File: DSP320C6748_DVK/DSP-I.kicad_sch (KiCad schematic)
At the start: 37 parts, among them IC1 SN74LVC1G11DBVR, J1 USB_A, J2 JTAG, U1 TMS320C6748EZWT4, Y1 ASE-24.000MHZ-LC-T, Y2 FX135A-327

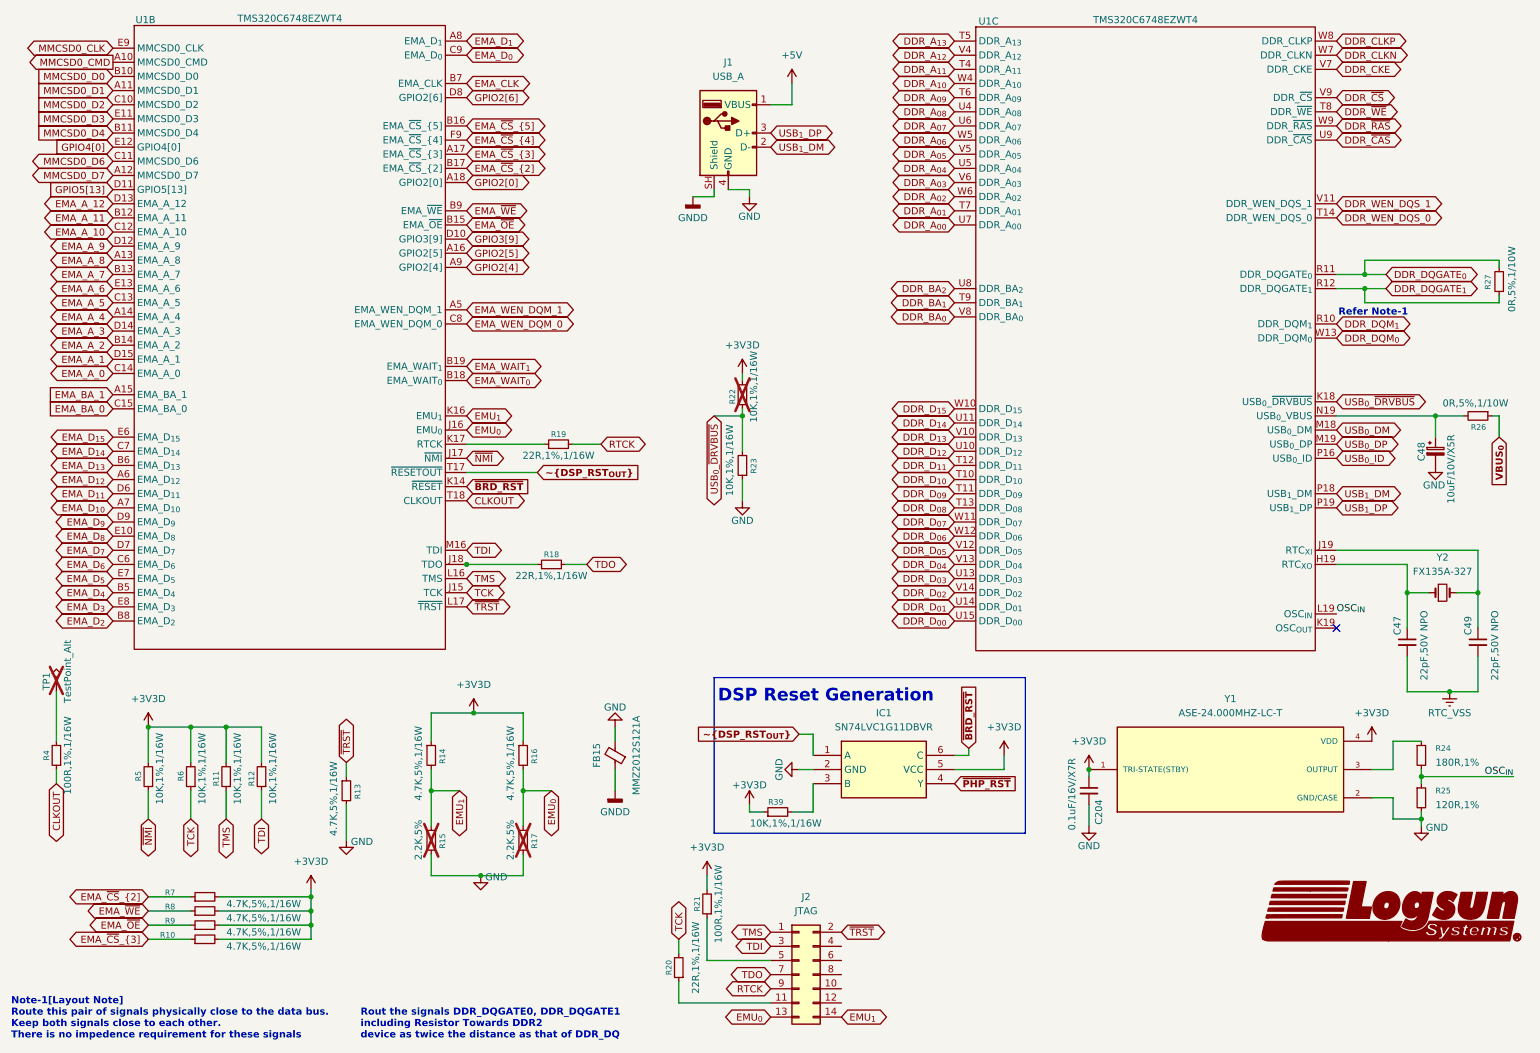
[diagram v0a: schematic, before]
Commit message: DC jack Replaced With Type-C, ADC and RTC section added
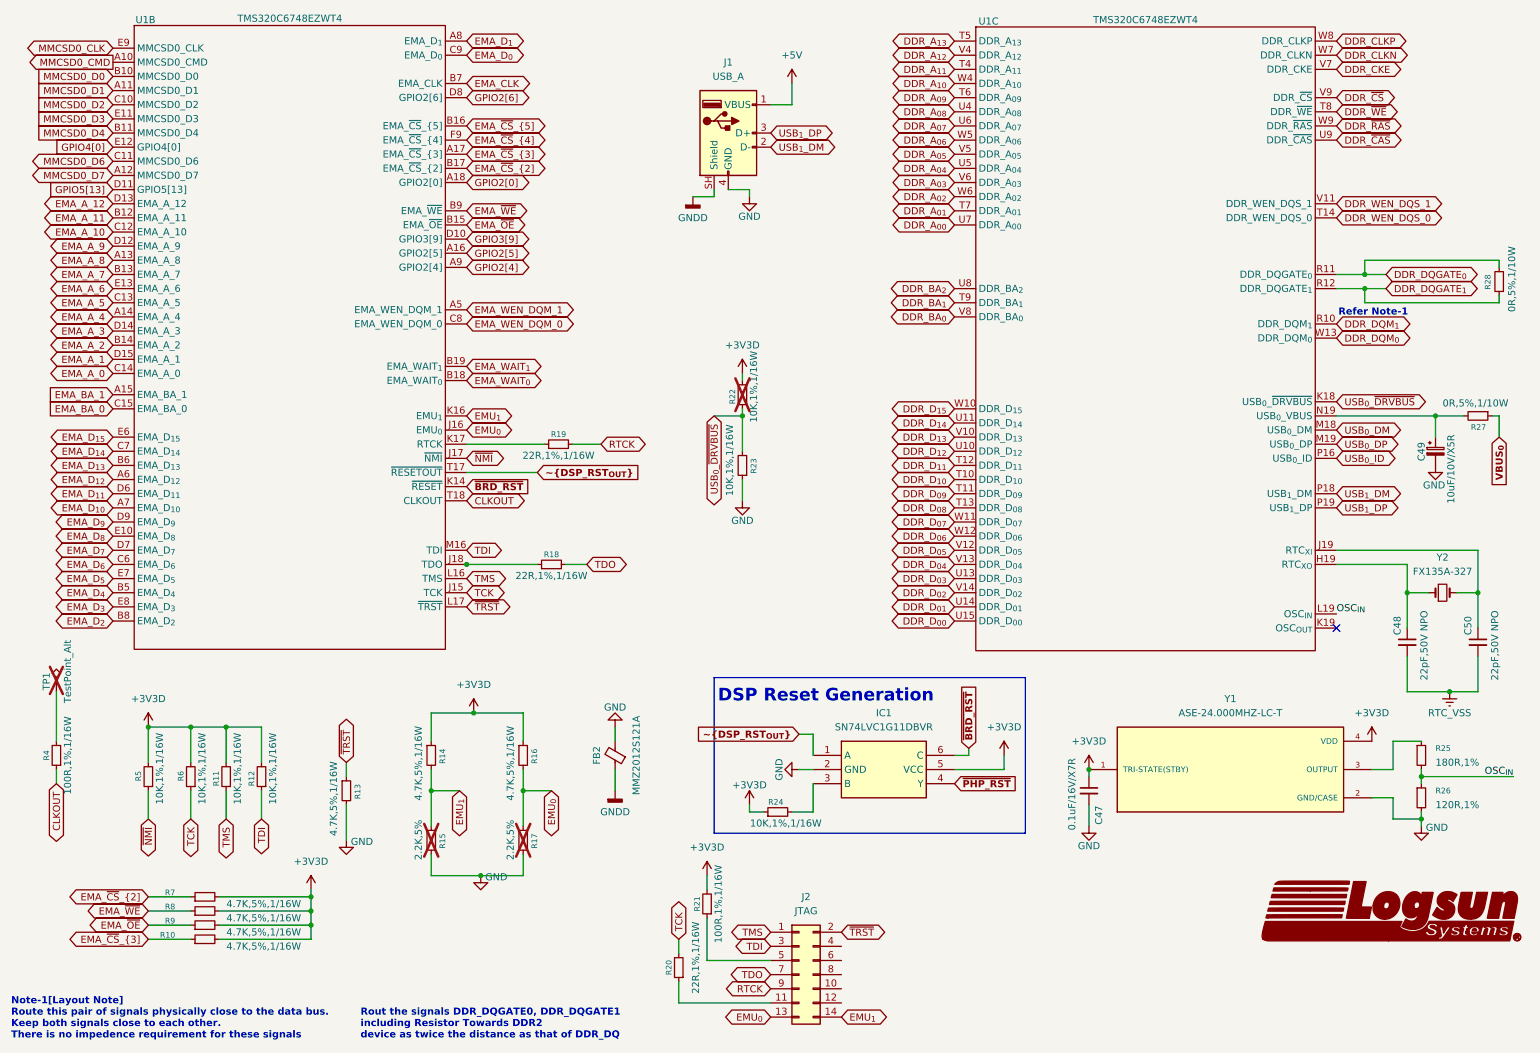
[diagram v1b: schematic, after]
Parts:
- renumbered C204 to C47, C47 to C48, C48 to C49, C49 to C50, FB15 to FB2, R39 to R24, R24 to R25, R25 to R26, R26 to R27, R27 to R28
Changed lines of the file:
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@@
 		(dnp no)
 		(fields_autoplaced yes)
-		(property "Reference" "#PWR035"
+		(property "Reference" "#PWR037"
 			(at 134.62 52.07 0)
 			(hide yes)
@@
 			(project "DSP320C6748_DVK"
 				(path "/3a70ffc0-9fe7-4a5b-b3c2-23140355df82/7f99a773-2324-4d25-8796-c695cf33a83f"
-					(reference "#PWR035")
+					(reference "#PWR037")
 					(unit 1)
 				)
@@
 		(dnp no)
 		(fields_autoplaced yes)
-		(property "Reference" "#PWR042"
+		(property "Reference" "#PWR048"
 			(at 256.54 147.32 0)
 			(hide yes)
@@
 			(project "DSP320C6748_DVK"
 				(path "/3a70ffc0-9fe7-4a5b-b3c2-23140355df82/7f99a773-2324-4d25-8796-c695cf33a83f"
-					(reference "#PWR042")
+					(reference "#PWR048")
 					(unit 1)
 				)
@@
 		(in_pos_files yes)
 		(dnp no)
-		(property "Reference" "#PWR048"
+		(property "Reference" "#PWR042"
 			(at 144.78 158.75 0)
 			(hide yes)
@@
 			(project "DSP320C6748_DVK"
 				(path "/3a70ffc0-9fe7-4a5b-b3c2-23140355df82/7f99a773-2324-4d25-8796-c695cf33a83f"
-					(reference "#PWR048")
+					(reference "#PWR042")
 					(unit 1)
 				)
@@
 		(in_pos_files yes)
 		(dnp no)
-		(property "Reference" "C49"
+		(property "Reference" "C50"
 			(at 273.812 124.46 90)
 			(show_name no)
@@
 			(project "DSP320C6748_DVK"
 				(path "/3a70ffc0-9fe7-4a5b-b3c2-23140355df82/7f99a773-2324-4d25-8796-c695cf33a83f"
-					(reference "C49")
+					(reference "C50")
 					(unit 1)
 				)
@@
 		(in_pos_files yes)
 		(dnp no)
-		(property "Reference" "#PWR043"
+		(property "Reference" "#PWR049"
 			(at 265.43 165.1 0)
 			(hide yes)
@@
 			(project "DSP320C6748_DVK"
 				(path "/3a70ffc0-9fe7-4a5b-b3c2-23140355df82/7f99a773-2324-4d25-8796-c695cf33a83f"
-					(reference "#PWR043")
+					(reference "#PWR049")
 					(unit 1)
 				)
@@
 		(dnp no)
 		(fields_autoplaced yes)
-		(property "Reference" "#PWR041"
+		(property "Reference" "#PWR046"
 			(at 205.74 152.4 0)
 			(hide yes)
@@
 			(project "DSP320C6748_DVK"
 				(path "/3a70ffc0-9fe7-4a5b-b3c2-23140355df82/7f99a773-2324-4d25-8796-c695cf33a83f"
-					(reference "#PWR041")
+					(reference "#PWR046")
 					(unit 1)
 				)
@@
 		(in_pos_files yes)
 		(dnp no)
-		(property "Reference" "R27"
+		(property "Reference" "R28"
 			(at 277.368 59.69 90)
 			(show_name no)
@@
 			(project "DSP320C6748_DVK"
 				(path "/3a70ffc0-9fe7-4a5b-b3c2-23140355df82/7f99a773-2324-4d25-8796-c695cf33a83f"
-					(reference "R27")
+					(reference "R28")
 					(unit 1)
 				)
@@
 		(dnp no)
 		(fields_autoplaced yes)
-		(property "Reference" "#PWR036"
+		(property "Reference" "#PWR038"
 			(at 137.16 171.45 0)
 			(hide yes)
@@
 			(project "DSP320C6748_DVK"
 				(path "/3a70ffc0-9fe7-4a5b-b3c2-23140355df82/7f99a773-2324-4d25-8796-c695cf33a83f"
-					(reference "#PWR036")
+					(reference "#PWR038")
 					(unit 1)
 				)
@@
 		(in_pos_files yes)
 		(dnp no)
-		(property "Reference" "FB15"
+		(property "Reference" "FB2"
 			(at 117.348 146.05 90)
 			(show_name no)
@@
 			(project "DSP320C6748_DVK"
 				(path "/3a70ffc0-9fe7-4a5b-b3c2-23140355df82/7f99a773-2324-4d25-8796-c695cf33a83f"
-					(reference "FB15")
+					(reference "FB2")
 					(unit 1)
 				)
@@
 		(dnp no)
 		(fields_autoplaced yes)
-		(property "Reference" "R25"
+		(property "Reference" "R26"
 			(at 267.97 152.3999 0)
 			(show_name no)
@@
 			(project "DSP320C6748_DVK"
 				(path "/3a70ffc0-9fe7-4a5b-b3c2-23140355df82/7f99a773-2324-4d25-8796-c695cf33a83f"
-					(reference "R25")
+					(reference "R26")
 					(unit 1)
 				)
@@
 		(in_pos_files yes)
 		(dnp no)
-		(property "Reference" "R26"
+		(property "Reference" "R27"
 			(at 274.32 87.122 90)
 			(show_name no)
@@
 			(project "DSP320C6748_DVK"
 				(path "/3a70ffc0-9fe7-4a5b-b3c2-23140355df82/7f99a773-2324-4d25-8796-c695cf33a83f"
-					(reference "R26")
+					(reference "R27")
 					(unit 1)
 				)
@@
 		(in_pos_files yes)
 		(dnp no)
-		(property "Reference" "C47"
+		(property "Reference" "C48"
 			(at 261.112 124.46 90)
 			(show_name no)
@@
 			(project "DSP320C6748_DVK"
 				(path "/3a70ffc0-9fe7-4a5b-b3c2-23140355df82/7f99a773-2324-4d25-8796-c695cf33a83f"
-					(reference "C47")
+					(reference "C48")
 					(unit 1)
 				)
@@
 		(in_pos_files yes)
 		(dnp no)
-		(property "Reference" "C48"
+		(property "Reference" "C49"
 			(at 265.43 93.218 90)
 			(show_name no)
@@
 			(project "DSP320C6748_DVK"
 				(path "/3a70ffc0-9fe7-4a5b-b3c2-23140355df82/7f99a773-2324-4d25-8796-c695cf33a83f"
-					(reference "C48")
+					(reference "C49")
 					(unit 1)
 				)
@@
 		(in_pos_files yes)
 		(dnp no)
-		(property "Reference" "#PWR049"
+		(property "Reference" "#PWR044"
 			(at 147.32 148.59 0)
 			(hide yes)
@@
 			(project "DSP320C6748_DVK"
 				(path "/3a70ffc0-9fe7-4a5b-b3c2-23140355df82/7f99a773-2324-4d25-8796-c695cf33a83f"
-					(reference "#PWR049")
+					(reference "#PWR044")
 					(unit 1)
 				)
@@
 		(in_pos_files yes)
 		(dnp no)
-		(property "Reference" "C204"
+		(property "Reference" "C47"
 			(at 207.518 158.496 90)
 			(show_name no)
@@
 			(project "DSP320C6748_DVK"
 				(path "/3a70ffc0-9fe7-4a5b-b3c2-23140355df82/7f99a773-2324-4d25-8796-c695cf33a83f"
-					(reference "C204")
+					(reference "C47")
 					(unit 1)
 				)
@@
 		(dnp no)
 		(fields_autoplaced yes)
-		(property "Reference" "#PWR038"
+		(property "Reference" "#PWR043"
 			(at 152.4 29.21 0)
 			(hide yes)
@@
 			(project "DSP320C6748_DVK"
 				(path "/3a70ffc0-9fe7-4a5b-b3c2-23140355df82/7f99a773-2324-4d25-8796-c695cf33a83f"
-					(reference "#PWR038")
+					(reference "#PWR043")
 					(unit 1)
 				)
@@
 		(in_pos_files yes)
 		(dnp no)
-		(property "Reference" "#PWR045"
+		(property "Reference" "#PWR051"
 			(at 270.51 140.97 0)
 			(hide yes)
@@
 			(project "DSP320C6748_DVK"
 				(path "/3a70ffc0-9fe7-4a5b-b3c2-23140355df82/7f99a773-2324-4d25-8796-c695cf33a83f"
-					(reference "#PWR045")
+					(reference "#PWR051")
 					(unit 1)
 				)
@@
 		(in_pos_files yes)
 		(dnp no)
-		(property "Reference" "#PWR0382"
+		(property "Reference" "#PWR035"
 			(at 120.65 134.62 0)
 			(hide yes)
@@
 			(project "DSP320C6748_DVK"
 				(path "/3a70ffc0-9fe7-4a5b-b3c2-23140355df82/7f99a773-2324-4d25-8796-c695cf33a83f"
-					(reference "#PWR0382")
+					(reference "#PWR035")
 					(unit 1)
 				)
@@
 		(dnp no)
 		(fields_autoplaced yes)
-		(property "Reference" "#PWR056"
+		(property "Reference" "#PWR045"
 			(at 190.5 149.86 0)
 			(hide yes)
@@
 			(project "DSP320C6748_DVK"
 				(path "/3a70ffc0-9fe7-4a5b-b3c2-23140355df82/7f99a773-2324-4d25-8796-c695cf33a83f"
-					(reference "#PWR056")
+					(reference "#PWR045")
 					(unit 1)
 				)
@@
 		(in_pos_files yes)
 		(dnp no)
-		(property "Reference" "#PWR0383"
+		(property "Reference" "#PWR047"
 			(at 205.74 165.1 0)
 			(hide yes)
@@
 			(project "DSP320C6748_DVK"
 				(path "/3a70ffc0-9fe7-4a5b-b3c2-23140355df82/7f99a773-2324-4d25-8796-c695cf33a83f"
-					(reference "#PWR0383")
+					(reference "#PWR047")
 					(unit 1)
 				)
@@
 		(dnp no)
 		(fields_autoplaced yes)
-		(property "Reference" "R24"
+		(property "Reference" "R25"
 			(at 267.97 144.7799 0)
 			(show_name no)
@@
 			(project "DSP320C6748_DVK"
 				(path "/3a70ffc0-9fe7-4a5b-b3c2-23140355df82/7f99a773-2324-4d25-8796-c695cf33a83f"
-					(reference "R24")
+					(reference "R25")
 					(unit 1)
 				)
@@
 		(dnp no)
 		(fields_autoplaced yes)
-		(property "Reference" "#PWR0381"
+		(property "Reference" "#PWR036"
 			(at 120.65 158.75 0)
 			(hide yes)
@@
 			(project "DSP320C6748_DVK"
 				(path "/3a70ffc0-9fe7-4a5b-b3c2-23140355df82/7f99a773-2324-4d25-8796-c695cf33a83f"
-					(reference "#PWR0381")
+					(reference "#PWR036")
 					(unit 1)
 				)
@@
 		(in_pos_files yes)
 		(dnp no)
-		(property "Reference" "R39"
+		(property "Reference" "R24"
 			(at 150.876 154.432 90)
 			(show_name no)
@@
 			(project "DSP320C6748_DVK"
 				(path "/3a70ffc0-9fe7-4a5b-b3c2-23140355df82/7f99a773-2324-4d25-8796-c695cf33a83f"
-					(reference "R39")
+					(reference "R24")
 					(unit 1)
 				)
@@
 		(in_pos_files yes)
 		(dnp no)
-		(property "Reference" "#PWR044"
+		(property "Reference" "#PWR050"
 			(at 267.97 100.33 0)
 			(hide yes)
@@
 			(project "DSP320C6748_DVK"
 				(path "/3a70ffc0-9fe7-4a5b-b3c2-23140355df82/7f99a773-2324-4d25-8796-c695cf33a83f"
-					(reference "#PWR044")
+					(reference "#PWR050")
 					(unit 1)
 				)
@@
 		(in_pos_files yes)
 		(dnp no)
-		(property "Reference" "#PWR037"
+		(property "Reference" "#PWR041"
 			(at 144.78 52.07 0)
 			(hide yes)
@@
 			(project "DSP320C6748_DVK"
 				(path "/3a70ffc0-9fe7-4a5b-b3c2-23140355df82/7f99a773-2324-4d25-8796-c695cf33a83f"
-					(reference "#PWR037")
+					(reference "#PWR041")
 					(unit 1)
 				)

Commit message: Scheamtic Re-annotation done, Some footprints assigned
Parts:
- C47, C48, C49, C50: footprint (none) -> Capacitor_SMD:C_0603_1608Metric_Pad1.08x0.95mm_HandSolder
- FB2: footprint (none) -> Inductor_SMD:L_0805_2012Metric_Pad1.05x1.20mm_HandSolder
- R10, R11, R12, R13, R14, R15, R16, R17, R18, R19, R20, R21, R22, R23, R24, R25, R26, R27, R28, R4, R5, R6, R7, R8, R9: footprint (none) -> Resistor_SMD:R_0603_1608Metric_Pad0.98x0.95mm_HandSolder
- TP1: footprint (none) -> TestPoint:TestPoint_Pad_D3.0mm
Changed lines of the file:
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@@
 			)
 		)
-		(property "Footprint" ""
+		(property "Footprint" "Resistor_SMD:R_0603_1608Metric_Pad0.98x0.95mm_HandSolder"
 			(at 57.15 149.86 0)
 			(hide yes)
@@
 			)
 		)
-		(property "Footprint" ""
+		(property "Footprint" "Resistor_SMD:R_0603_1608Metric_Pad0.98x0.95mm_HandSolder"
 			(at 20.32 146.05 0)
 			(hide yes)
@@
 			)
 		)
-		(property "Footprint" ""
+		(property "Footprint" "Resistor_SMD:R_0603_1608Metric_Pad0.98x0.95mm_HandSolder"
 			(at 72.39 152.4 0)
 			(hide yes)
@@
 			)
 		)
-		(property "Footprint" ""
+		(property "Footprint" "Resistor_SMD:R_0603_1608Metric_Pad0.98x0.95mm_HandSolder"
 			(at 104.14 161.29 0)
 			(hide yes)
@@
 			)
 		)
-		(property "Footprint" ""
+		(property "Footprint" "Capacitor_SMD:C_0603_1608Metric_Pad1.08x0.95mm_HandSolder"
 			(at 275.59 125.73 0)
 			(hide yes)
@@
 			)
 		)
-		(property "Footprint" ""
+		(property "Footprint" "Resistor_SMD:R_0603_1608Metric_Pad0.98x0.95mm_HandSolder"
 			(at 137.16 172.72 0)
 			(hide yes)
@@
 			)
 		)
-		(property "Footprint" ""
+		(property "Footprint" "Resistor_SMD:R_0603_1608Metric_Pad0.98x0.95mm_HandSolder"
 			(at 44.45 149.86 0)
 			(hide yes)
@@
 			)
 		)
-		(property "Footprint" ""
+		(property "Footprint" "Resistor_SMD:R_0603_1608Metric_Pad0.98x0.95mm_HandSolder"
 			(at 109.22 111.76 0)
 			(hide yes)
@@
 			)
 		)
-		(property "Footprint" ""
+		(property "Footprint" "Resistor_SMD:R_0603_1608Metric_Pad0.98x0.95mm_HandSolder"
 			(at 36.83 149.86 0)
 			(hide yes)
@@
 			)
 		)
-		(property "Footprint" ""
+		(property "Footprint" "Resistor_SMD:R_0603_1608Metric_Pad0.98x0.95mm_HandSolder"
 			(at 143.51 81.28 0)
 			(hide yes)
@@
 			)
 		)
-		(property "Footprint" ""
+		(property "Footprint" "Resistor_SMD:R_0603_1608Metric_Pad0.98x0.95mm_HandSolder"
 			(at 279.4 60.96 0)
 			(hide yes)
@@
 			)
 		)
-		(property "Footprint" ""
+		(property "Footprint" "Resistor_SMD:R_0603_1608Metric_Pad0.98x0.95mm_HandSolder"
 			(at 87.63 146.05 0)
 			(hide yes)
@@
 			)
 		)
-		(property "Footprint" ""
+		(property "Footprint" "Resistor_SMD:R_0603_1608Metric_Pad0.98x0.95mm_HandSolder"
 			(at 46.99 176.53 0)
 			(hide yes)
@@
 			)
 		)
-		(property "Footprint" ""
+		(property "Footprint" "Resistor_SMD:R_0603_1608Metric_Pad0.98x0.95mm_HandSolder"
 			(at 132.08 184.15 0)
 			(hide yes)
@@
 			)
 		)
-		(property "Footprint" ""
+		(property "Footprint" "Inductor_SMD:L_0805_2012Metric_Pad1.05x1.20mm_HandSolder"
 			(at 122.428 146.05 90)
 			(hide yes)
@@
 			)
 		)
-		(property "Footprint" ""
+		(property "Footprint" "Resistor_SMD:R_0603_1608Metric_Pad0.98x0.95mm_HandSolder"
 			(at 87.63 161.29 0)
 			(hide yes)
@@
 			)
 		)
-		(property "Footprint" ""
+		(property "Footprint" "Resistor_SMD:R_0603_1608Metric_Pad0.98x0.95mm_HandSolder"
 			(at 46.99 179.07 0)
 			(hide yes)
@@
 			)
 		)
-		(property "Footprint" ""
+		(property "Footprint" "Resistor_SMD:R_0603_1608Metric_Pad0.98x0.95mm_HandSolder"
 			(at 265.43 153.67 0)
 			(hide yes)
@@
 			)
 		)
-		(property "Footprint" ""
+		(property "Footprint" "Resistor_SMD:R_0603_1608Metric_Pad0.98x0.95mm_HandSolder"
 			(at 143.51 93.98 0)
 			(hide yes)
@@
 			)
 		)
-		(property "Footprint" ""
+		(property "Footprint" "TestPoint:TestPoint_Pad_D3.0mm"
 			(at 25.4 134.62 0)
 			(hide yes)
@@
 			)
 		)
-		(property "Footprint" ""
+		(property "Footprint" "Resistor_SMD:R_0603_1608Metric_Pad0.98x0.95mm_HandSolder"
 			(at 46.99 171.45 0)
 			(hide yes)
@@
 			)
 		)
-		(property "Footprint" ""
+		(property "Footprint" "Resistor_SMD:R_0603_1608Metric_Pad0.98x0.95mm_HandSolder"
 			(at 275.59 85.09 0)
 			(hide yes)
@@
 			)
 		)
-		(property "Footprint" ""
+		(property "Footprint" "Capacitor_SMD:C_0603_1608Metric_Pad1.08x0.95mm_HandSolder"
 			(at 262.89 125.73 0)
 			(hide yes)
@@
 			)
 		)
-		(property "Footprint" ""
+		(property "Footprint" "Capacitor_SMD:C_0603_1608Metric_Pad1.08x0.95mm_HandSolder"
 			(at 267.97 91.44 0)
 			(hide yes)
@@
 			)
 		)
-		(property "Footprint" ""
+		(property "Footprint" "Resistor_SMD:R_0603_1608Metric_Pad0.98x0.95mm_HandSolder"
 			(at 46.99 173.99 0)
 			(hide yes)
@@
 			)
 		)
-		(property "Footprint" ""
+		(property "Footprint" "Capacitor_SMD:C_0603_1608Metric_Pad1.08x0.95mm_HandSolder"
 			(at 205.74 152.4 0)
 			(hide yes)
@@
 			)
 		)
-		(property "Footprint" ""
+		(property "Footprint" "Resistor_SMD:R_0603_1608Metric_Pad0.98x0.95mm_HandSolder"
 			(at 265.43 146.05 0)
 			(hide yes)
@@
 			)
 		)
-		(property "Footprint" ""
+		(property "Footprint" "Resistor_SMD:R_0603_1608Metric_Pad0.98x0.95mm_HandSolder"
 			(at 149.86 156.21 0)
 			(hide yes)
@@
 			)
 		)
-		(property "Footprint" ""
+		(property "Footprint" "Resistor_SMD:R_0603_1608Metric_Pad0.98x0.95mm_HandSolder"
 			(at 104.14 146.05 0)
 			(hide yes)
@@
 			)
 		)
-		(property "Footprint" ""
+		(property "Footprint" "Resistor_SMD:R_0603_1608Metric_Pad0.98x0.95mm_HandSolder"
 			(at 110.49 90.17 0)
 			(hide yes)
@@
 			)
 		)
-		(property "Footprint" ""
+		(property "Footprint" "Resistor_SMD:R_0603_1608Metric_Pad0.98x0.95mm_HandSolder"
 			(at 50.8 149.86 0)
 			(hide yes)
